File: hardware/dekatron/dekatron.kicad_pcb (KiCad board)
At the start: 2 copper layers, 100 x 85 mm, 164 parts, among them J101 PWR_IN, J102 NIX_12V, J201 TUBE_ANODE, J202 TUBE, J301 DISP, J302 NIX_LV, Q101 AOD4185, Q102 AOD5N40, Q201 MMBTA42, Q202 MMBTA42, Q203 MMBTA92, U101 TPS54202, U102 LM66100, U103 LM66100, U104 LM66100, U105 LP2951 (adj. 10 V), U106 LM5156H, U107 TLV3011, U108 TLV3011, U301 RP2040-Zero

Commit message: Swap AOS MOSFETs for Mouser-stocked Infineon parts
Q101 AOD4185 -> IPD50P04P4L-11 (-40 V, 10.6 mohm, 200 A pulsed, VGS +5/-16 V);
input_protect re-run with its resistance: inrush 52.5 A, rail 12.6 V, fuse
I2t 0.089 A2s, VGS -9.97..+0.14 V, reversal blocked.
Q102 AOD5N40 -> IPD50R1K4CE (500 V CoolMOS CE, 1.4 ohm, Vth 2.5-3.5 V): margin
2.56x on the 195 V worst case; figures from distributor listings, flagged to
confirm against Infineon's datasheet.
Same DPAK footprint and pinout; PCB fields updated in place, DRC parity clean.
Fab outputs unchanged (no part values in them).

Co-Authored-By: Claude Opus 5.5 <noreply@anthropic.com>
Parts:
- Q101: value AOD4185 -> IPD50P04P4L-11
- Q102: value AOD5N40 -> IPD50R1K4CE
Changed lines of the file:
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@@
 			)
 		)
-		(property "Value" "AOD5N40"
+		(property "Value" "IPD50R1K4CE"
 			(at 0 4.5 0)
 			(layer "F.Fab")
@@
 			)
 		)
-		(property "MPN" "AOD5N40"
+		(property "MPN" "IPD50R1K4CE"
 			(at 0 0 0)
 			(layer "F.SilkS")
@@
 			)
 		)
-		(property "Manufacturer" "Alpha & Omega"
+		(property "Manufacturer" "Infineon"
 			(at 0 0 0)
 			(layer "F.SilkS")
@@
 			)
 		)
-		(property "Rating" "400 V, 1.6 ohm at 10 V"
+		(property "Rating" "500 V, 1.4 ohm at 10 V"
 			(at 0 0 0)
 			(layer "F.SilkS")
@@
 			)
 		)
-		(property "Value" "AOD4185"
+		(property "Value" "IPD50P04P4L-11"
 			(at 0 4.5 0)
 			(layer "F.Fab")
@@
 			)
 		)
-		(property "MPN" "AOD4185"
+		(property "MPN" "IPD50P04P4L-11"
 			(at 0 0 0)
 			(layer "F.SilkS")
@@
 			)
 		)
-		(property "Manufacturer" "Alpha & Omega"
+		(property "Manufacturer" "Infineon"
 			(at 0 0 0)
 			(layer "F.SilkS")
@@
 			)
 		)
-		(property "Rating" "-40 V, 115 A pulsed"
+		(property "Rating" "-40 V, 10.6 mohm, 200 A pulsed, VGS +5/-16 V"
 			(at 0 0 0)
 			(layer "F.SilkS")

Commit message: Use E12 values for the Yageo HHV high-voltage resistors
HHV stock at Mouser follows E12 (2.2M/2.7M stocked, 2.0M/2.4M/332k not).
HHV parts now: 4.7M x2 (feedback, monitor/OVP tops), 2.2M x2 (V_b bleeder,
V_b OVP top), 220k (index), 330k x2 (anode, = D1's 660k design value);
R202 stays 200k (stocked, already ordered). Trims moved to 1206 bottoms:
feedback 10.4k -> 452.9 V (9.53k: 494.2 V); OVP 10.7k -> 548.4 V trip,
HV_SENSE = HV/191.3; V_b OVP 13.7k -> 200.7 V. 500 V anode option 330k +
470k = 800k; off-board dummy load 1M.

Re-simulated: 500 V setting regulates at 494.1 V out of current limit
(tube 368 uA, peaks HV 498 V, V_b 170 V); dark-tube feedback-open fault trips
at 550.3 V, bursts 547.1-549.7 V; open tripler diode holds V_b <= 198.4 V;
discharge < 50 V in 1.94 / 3.93 / 3.47 s. PCB fields synced, ERC/DRC
parity unchanged; footprints and fab files unchanged.

Co-Authored-By: Claude Opus 5.5 <noreply@anthropic.com>
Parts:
- R119: value 2.4M -> 2.2M
- R126: value 4.75M -> 4.7M
- R130: value 10.5k -> 10.4k
- R131: value 4.64M -> 4.7M
- R140: value 10.5k -> 10.7k
- R141: value 2.0M -> 2.2M
- R143: value 12.4k -> 13.7k
- R215, R216: value 332k -> 330k
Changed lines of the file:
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@@
 			)
 		)
-		(property "Value" "332k"
+		(property "Value" "330k"
 			(at 7.62 2.92 180)
 			(layer "F.Fab")
@@
 			)
 		)
-		(property "MPN" "HHV-50FT-52-332K"
+		(property "MPN" "HHV-50FT-52-330K"
 			(at 0 0 180)
 			(layer "F.SilkS")
@@
 			)
 		)
-		(property "Value" "332k"
+		(property "Value" "330k"
 			(at 7.62 2.92 0)
 			(layer "F.Fab")
@@
 			)
 		)
-		(property "MPN" "HHV-50FT-52-332K"
+		(property "MPN" "HHV-50FT-52-330K"
 			(at 0 0 0)
 			(layer "F.SilkS")
@@
 			)
 		)
-		(property "Value" "2.0M"
+		(property "Value" "2.2M"
 			(at 5.08 2.37 180)
 			(layer "F.Fab")
@@
 			)
 		)
-		(property "MPN" "HHV-25FT-52-2M"
+		(property "MPN" "HHV-25FT-52-2M2"
 			(at 0 0 180)
 			(layer "F.SilkS")
@@
 			)
 		)
-		(property "Value" "10.5k"
+		(property "Value" "10.4k"
 			(at 0 1.83 0)
 			(layer "F.Fab")
@@
 			)
 		)
-		(property "Function" "HV feedback, lower (453.4 V; 9.53k for 500 V)"
+		(property "Function" "HV feedback, lower (452.9 V; 9.53k for 500 V: 494.2 V)"
 			(at 0 0 0)
 			(layer "F.SilkS")
@@
 			)
 		)
-		(property "Value" "12.4k"
+		(property "Value" "13.7k"
 			(at 0 1.83 90)
 			(layer "F.Fab")
@@
 			)
 		)
-		(property "Function" "V_b OVP divider, lower (trip ~202 V)"
+		(property "Function" "V_b OVP divider, lower (trip 200.7 V)"
 			(at 0 0 90)
 			(layer "F.SilkS")
@@
 			)
 		)
-		(property "Function" "HV monitor / OVP divider, middle (HV_SENSE 2.36 V at 450 V)"
+		(property "Function" "HV monitor / OVP divider, middle (HV_SENSE 2.37 V at 452.9 V)"
 			(at 0 0 180)
 			(layer "F.SilkS")
@@
 			)
 		)
-		(property "Value" "4.64M"
+		(property "Value" "4.7M"
 			(at 5.08 2.37 180)
 			(layer "F.Fab")
@@
 			)
 		)
-		(property "MPN" "HHV-25FT-52-4M64"
+		(property "MPN" "HHV-25FT-52-4M7"
 			(at 0 0 180)
 			(layer "F.SilkS")
@@
 			)
 		)
-		(property "Value" "10.5k"
+		(property "Value" "10.7k"
 			(at 0 1.83 90)
 			(layer "F.Fab")
@@
 			)
 		)
-		(property "Function" "HV monitor / OVP divider, lower (OVP trip 551.8 V)"
+		(property "Function" "HV monitor / OVP divider, lower (OVP trip 548.4 V)"
 			(at 0 0 90)
 			(layer "F.SilkS")
@@
 			)
 		)
-		(property "Value" "2.4M"
+		(property "Value" "2.2M"
 			(at 5.08 2.37 180)
 			(layer "F.Fab")
@@
 			)
 		)
-		(property "MPN" "HHV-25FT-52-2M4"
+		(property "MPN" "HHV-25FT-52-2M2"
 			(at 0 0 180)
 			(layer "F.SilkS")
@@
 			)
 		)
-		(property "Value" "4.75M"
+		(property "Value" "4.7M"
 			(at 5.08 2.37 180)
 			(layer "F.Fab")
@@
 			)
 		)
-		(property "MPN" "HHV-25FT-52-4M75"
+		(property "MPN" "HHV-25FT-52-4M7"
 			(at 0 0 180)
 			(layer "F.SilkS")

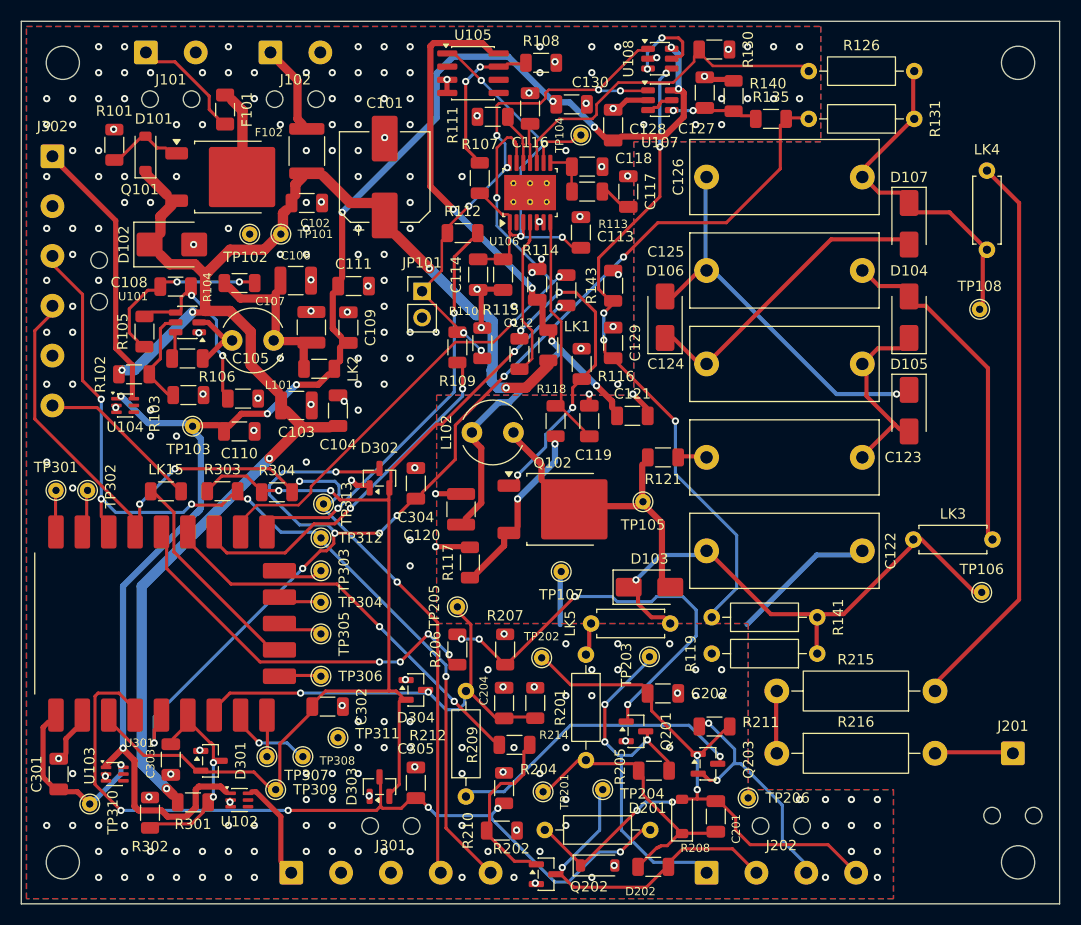
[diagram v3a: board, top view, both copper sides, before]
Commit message: Fix LM66100 reverse blocking (CE to VOUT); 2.7M HV divider tops; re-route
LM66100 (U102-U104): CE was grounded, the datasheet's always-on mode without
reverse-current blocking (SLVSEZ8A 8.3.1). CE now ties to VOUT (8.3.2, always-on
reverse current blocking); unused ST goes to GND as the pin table asks (three
expected ERC open-collector entries).

HV divider tops: HHV-25 4.7M had a 10-week lead time; one stocked 2.7M each
(0.11 W at 550 V). Feedback 2.7M / 5.97k -> 453.3 V (5.49k: 492.8 V); OVP
2.7M / 7.87k / 6.19k -> 544.6 V trip, HV_SENSE = HV/193.0. Re-simulated: 500 V
setting 492.7 V out of current limit (0.34 A of 0.43 A); dark-tube feedback-
open fault trips at 545.8 V; discharge < 50 V in 1.10 / 2.03 / 2.03 s.

Router: LM66100 CE-VOUT laid under the package body before routing, and fixed
GND escape vias for pins 2 and 5 (R301, C108 anchored 0.6 mm clear); 0.03 mm
extra margin against other nets' pads; vias keep 0.25 mm hole-to-hole from
plated holes. Converged on pass 5. DRC: 0 unconnected, 0 clearance, 0 parity;
expected U106 library mismatch and one U107 starved thermal. Fab outputs
regenerated (the previous set was not ordered).

Co-Authored-By: Claude Opus 5.5 <noreply@anthropic.com>
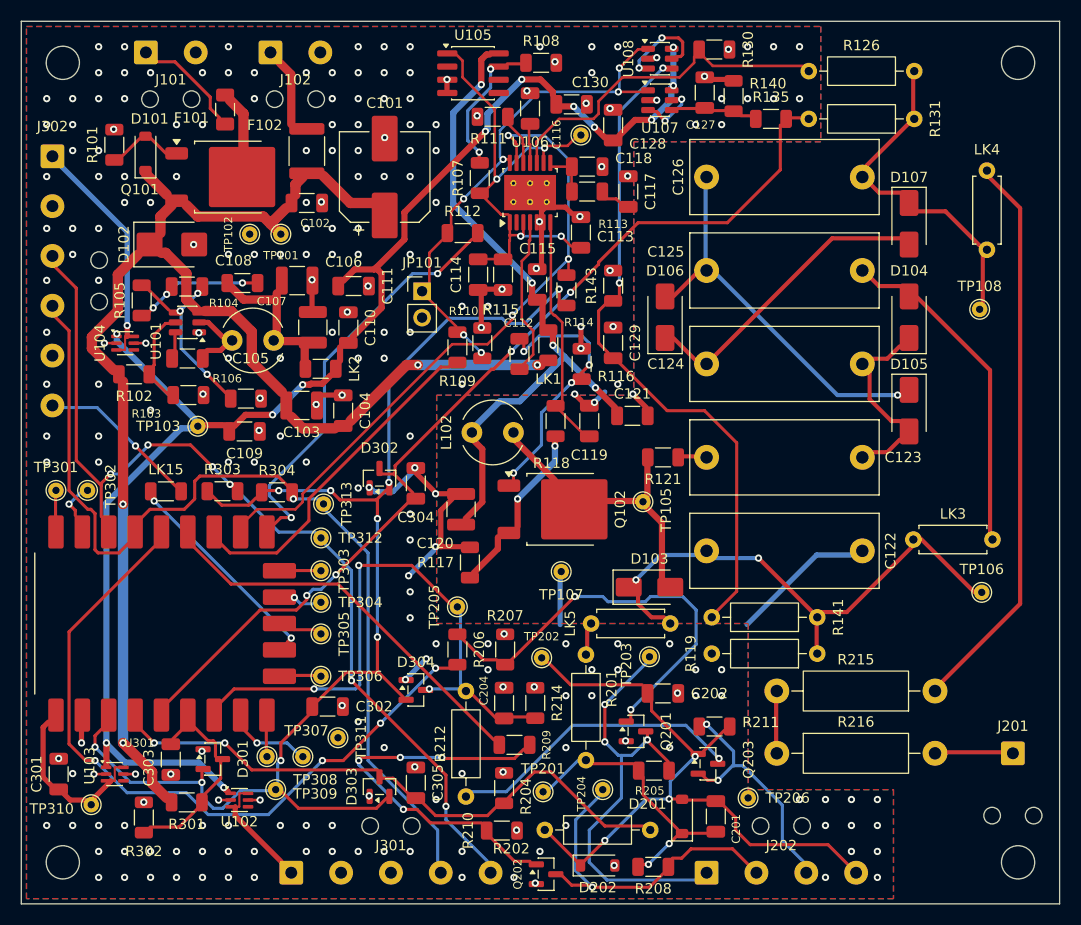
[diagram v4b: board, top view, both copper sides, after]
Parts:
- R126, R131: value 4.7M -> 2.7M
- R130: value 10.4k -> 5.97k
- R135: value 14.0k -> 7.87k
- R140: value 10.7k -> 6.19k
- moved C110 14.5 mm to (81.5, 79.5), turned to 90 degrees
- moved C109 14.1 mm to (71.5, 89.5), turned to 0 degrees
- moved U104 6.00 mm to (60.0, 81.0)
- moved R105 3.01 mm to (61.6, 76.9)
- moved C108 1.10 mm to (66.0, 75.5)
- moved R302 0.75 mm to (61.8, 126.7)
- moved R301 0.60 mm to (65.9, 125.2)
- moved C103 0.50 mm to (77.0, 87.0)
- moved C104 0.50 mm to (81.0, 87.5)
- moved TP103 0.50 mm to (67.0, 89.0)
- moved D301 0.28 mm to (68.4, 121.1)
- moved R106 0.28 mm to (71.6, 86.3)
- moved R104 0.28 mm to (71.3, 75.2)
- moved TP310 0.16 mm to (56.7, 125.4)
- moved C106 0.14 mm to (76.6, 75.0)
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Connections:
- U102 pad 3: GND -> 5V_DISP
- U102 pad 5: unconnected-(U102-ST-Pad5) -> GND
- U103 pad 3: GND -> 5V_MCU
- U103 pad 5: unconnected-(U103-ST-Pad5) -> GND
- U104 pad 3: GND -> 5V_NIX
- U104 pad 5: unconnected-(U104-ST-Pad5) -> GND
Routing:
- net GND: track 39.7 -> 73.9 mm, vias 243 -> 242
- net GUIDE1: track 35.5 -> 67.7 mm
- net /tube/G2_B: track 13.7 -> 35.7 mm, vias 0 -> 4
- net RTN_SENSE: track 73.7 -> 51.8 mm, vias 5 -> 2
- net HV_SENSE: track 111.7 -> 90.3 mm, vias 8 -> 4
- net +3V3: track 101.6 -> 118.3 mm, vias 4 -> 9
- net NDX: track 37.3 -> 50.5 mm, vias 2 -> 3
- net /tube/TUBE_G1: track 33.7 -> 40.6 mm
- net /power/12V_HV: track 65.2 -> 59.2 mm
- net +5V: track 138.6 -> 132.7 mm, vias 9 -> 12
- net /power/Q102_G: track 27.7 -> 23.1 mm
- net /power/BUCK_FBT: track 14.9 -> 10.8 mm, vias 2 -> 3
- net /mcu/SDA: track 85.5 -> 89.1 mm, vias 5 -> 6
- net /power/OVP_REF: track 1.47 -> 4.79 mm, vias 0 -> 2
- net 5V_NIX: track 25.0 -> 21.9 mm, vias 0 -> 1
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
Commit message: WIMA MKS4 film caps (18 x 8 mm) and EEE-FK1V101XP bulk cap; re-route
- C122-C126: WIMA MKS4G034704F00MSSD on the C_Rect L18 W8 P15 footprint;
  C126 moves 0.2 mm down to keep its courtyard off R131.
- C101: Panasonic EEE-FK1V101XP (6.3 x 7.7 mm, 340 mohm). input_protect.cir
  re-run: worst lead 12.0 V / 47.9 A / 0.070 A2s (was 12.5 V / 52.5 A / 0.088).
- Router: 0.05 mm extra clearance to other nets' tracks outside the LM5156
  pin group (DRC found a 0.153 mm VIN_PROT/PGOOD gap from raster error).
- DRC: 0 unconnected / 0 clearance / 0 parity; 2 expected findings.
  Fab outputs regenerated.

Co-Authored-By: Claude Opus 5.5 <noreply@anthropic.com>
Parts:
- C101: footprint Capacitor_SMD:CP_Elec_8x10.5 -> Capacitor_SMD:CP_Elec_6.3x7.7
- C122, C123, C124, C125, C126: footprint Capacitor_THT:C_Rect_L18.0mm_W7.0mm_P15.00mm_FKS3_FKP3 -> Capacitor_THT:C_Rect_L18.0mm_W8.0mm_P15.00mm_FKS3_FKP3
- moved LK3 8.02 mm to (136.4, 107.9), turned to 90 degrees
- moved U107 0.50 mm to (111.5, 57.1)
- moved U108 0.50 mm to (111.5, 53.1)
- moved C129 0.25 mm to (107.0, 80.7)
- moved R143 0.25 mm to (107.0, 75.2)
- moved C126 0.20 mm to (116.0, 65.2)
- moved C127 0.17 mm to (115.8, 56.7)
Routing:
- net GUIDE1: track 67.7 -> 31.7 mm, vias 4 -> 0
- net GND: track 73.9 -> 42.6 mm, vias 242 -> 239
- net /tube/G1_B: track 38.5 -> 16.3 mm, vias 2 -> 0
- net /tube/G2_B: track 35.7 -> 20.0 mm, vias 4 -> 2
- net NDX: track 50.5 -> 36.6 mm, vias 3 -> 5
- net /power/Q102_G: track 23.1 -> 31.7 mm
- net +5V: track 132.7 -> 124.2 mm, vias 12 -> 14
- net /mcu/SCL: track 85.7 -> 78.8 mm, vias 1 -> 4
- net /mcu/SDA: track 89.1 -> 96.0 mm, vias 6 -> 5
- net /tube/NDX_C: track 28.1 -> 33.7 mm
- net /power/V_B: track 42.8 -> 38.4 mm
- net PGOOD: track 61.4 -> 57.2 mm
- net /power/12V_HV: track 59.2 -> 63.3 mm, vias 4 -> 6
- net /power/HV_EN_PIN: track 42.5 -> 39.3 mm, vias 6 -> 4
- net GUIDE2: track 36.6 -> 39.8 mm
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
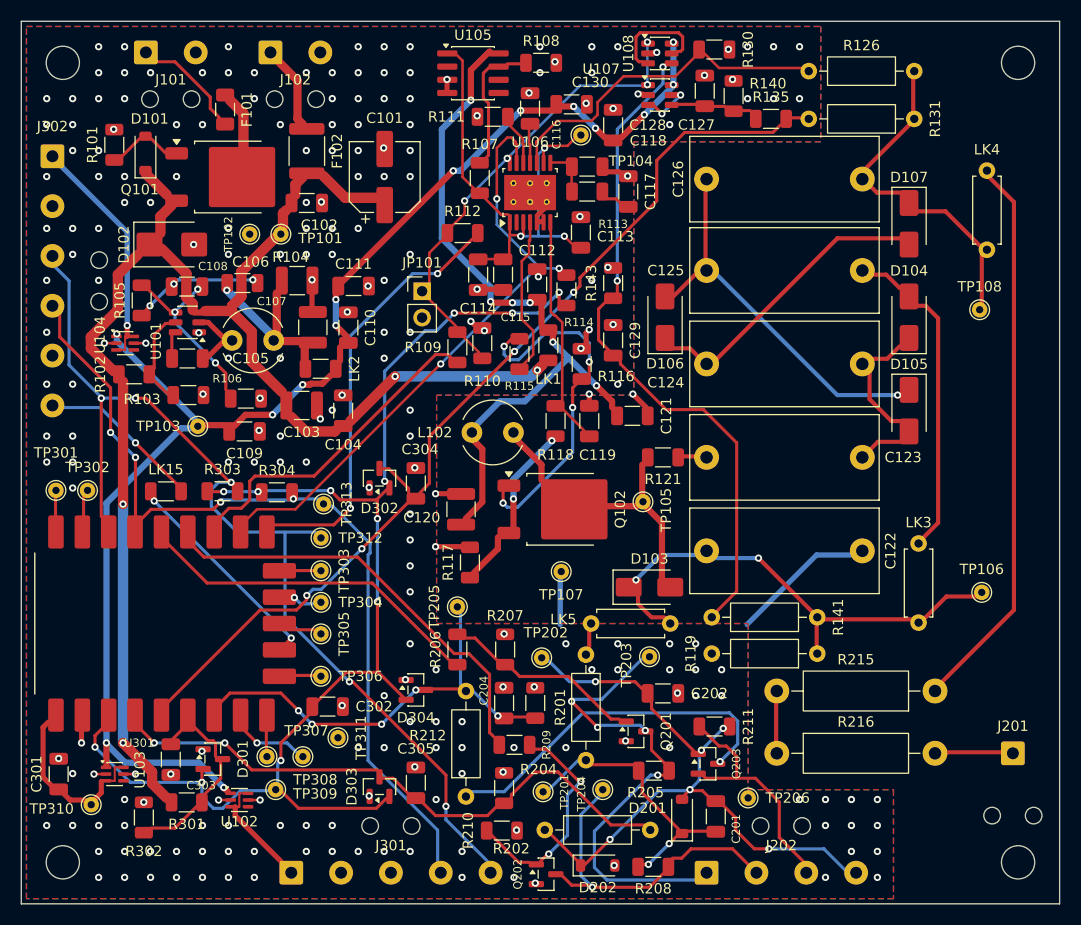
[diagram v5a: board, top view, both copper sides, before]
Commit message: Freeze the dekatron BOM to the Mouser order; substitutions; re-route
- ORDERED_PARTS in gen_schematics.py: exact manufacturer part numbers from
  Cart_Oct08_0432PM.xls (committed as the record), overriding design-time MPNs
- Backorder substitutions: TPS54302 (pin-compatible 5 V buck), IPD70R1K4P7S
  (700 V CoolMOS P7, replaces the EOL IPD50R1K4CE), MMSZ5262BT1G, BAT54S RFG
- C301 is the user's F91 tantalum: polarised symbol and EIA 3216-18 footprint
- E24 dividers: HV feedback 2 x 3.0k 0805 (451.0 V; 2 x 2.7k for 500 V),
  OVP lower 6.2k (543.7 V); simulations re-run, docs updated
- Router: exact own-pad clearance, D301 GND escape via kept out of the
  RP2040 no-via area (D301 anchored rotated), 0.3 mm GND repair links
- Full re-route, DRC clean (expected U106 mismatch, one starved thermal);
  fab outputs regenerated

Co-Authored-By: Claude Opus 5.5 <noreply@anthropic.com>
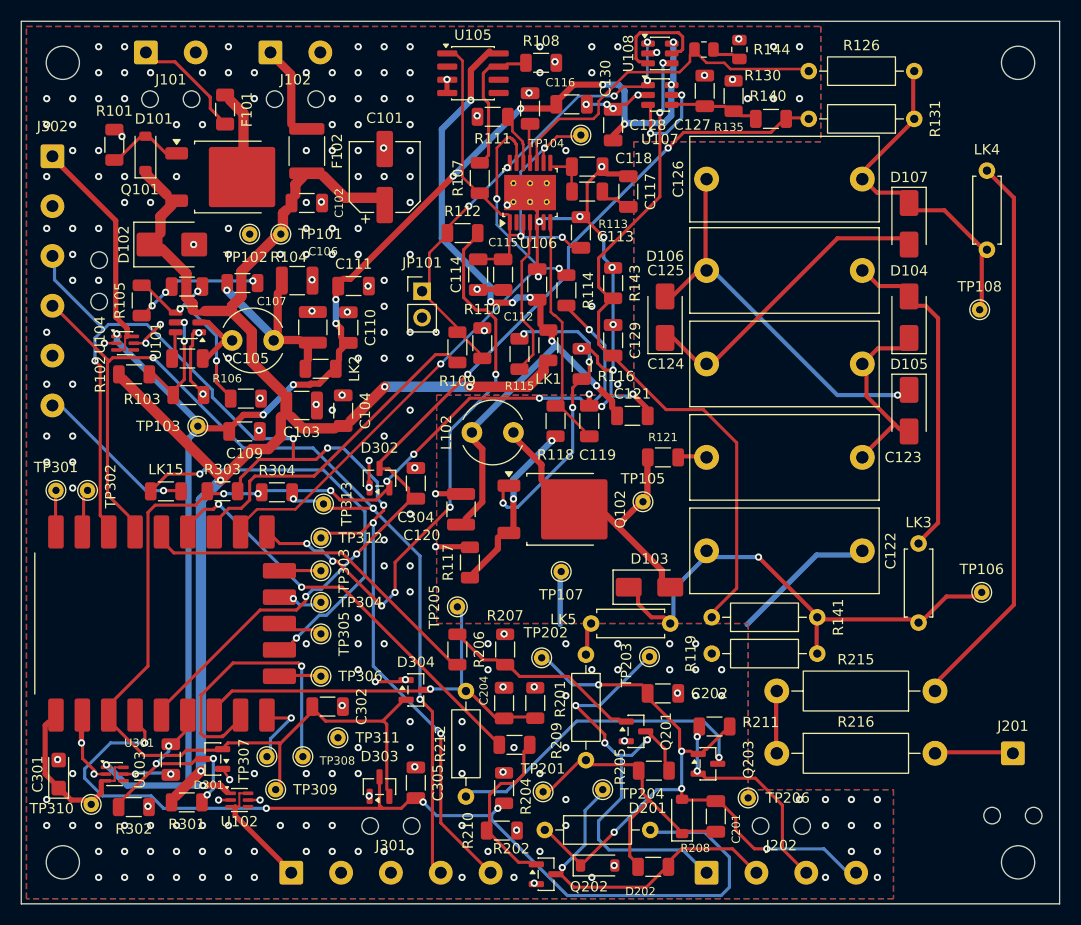
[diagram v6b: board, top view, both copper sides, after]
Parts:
- added R144: 3.0k, Resistor_SMD:R_0805_2012Metric, F.Cu at (119.2, 52.7)
- C301: footprint Capacitor_SMD:C_1206_3216Metric -> Capacitor_Tantalum_SMD:CP_EIA-3216-18_Kemet-A
- Q102: value IPD50R1K4CE -> IPD70R1K4P7S
- R130: value 5.97k -> 3.0k; footprint Resistor_SMD:R_1206_3216Metric -> Resistor_SMD:R_0805_2012Metric
- R140: value 6.19k -> 6.2k
- U101: value TPS54202 -> TPS54302
- moved R302 1.39 mm to (60.8, 125.7), turned to 0 degrees
- moved R130 1.00 mm to (115.7, 52.7)
- turned D301 to 180 degrees
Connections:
- R130 pad 2: GND -> Net-(R130-Pad2)
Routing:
- net GND: track 42.6 -> 103.4 mm, vias 239 -> 259
- net RTN_SENSE: track 51.7 -> 90.1 mm, vias 2 -> 4
- net /mcu/GP15: track 5.87 -> 26.5 mm
- net /mcu/SDA: track 96.0 -> 115.1 mm, vias 5 -> 6
- net /mcu/GP12: track 19.4 -> 38.4 mm
- net /mcu/SCL: track 78.8 -> 97.4 mm
- net OVP_TRIP: track 40.2 -> 55.1 mm, vias 2 -> 6
- net /tube/G2_B: track 20.0 -> 13.7 mm, vias 2 -> 0
- net /power/Q102_G: track 31.7 -> 26.9 mm
- net /power/OVP_REF: track 4.08 -> 8.92 mm
- net /tube/NDX_C: track 33.7 -> 29.6 mm
- net /mcu/GP14: track 1.80 -> 5.63 mm, vias 0 -> 1
- net +5V: track 124.2 -> 127.9 mm, vias 14 -> 13
- net /tube/TUBE_K1: track 21.5 -> 18.8 mm, vias 0 -> 2
- net NDX: track 36.6 -> 34.0 mm, vias 5 -> 1
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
